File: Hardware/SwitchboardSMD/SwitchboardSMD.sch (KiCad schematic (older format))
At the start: 40 parts, among them J2 S88_In_Plug, J4 S88_Out_Plug, Q1 BC237, SW1 SW_Push, SW2 SW_Push, SW3 SW_Push, SW4 SW_Push, SW5 SW_Push, SW6 SW_Push, SW7 SW_Push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

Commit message: Fixed IC footprints
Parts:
- U1, U2, U3: footprint Package_SO:SOP-16_4.55x10.3mm_P1.27mm -> Package_SO:SOIC-16_3.9x9.9mm_P1.27mm
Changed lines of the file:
@@
 F 0 "U1" H 5100 2816 50  0000 C CNN
 F 1 "4044" H 5100 2725 50  0000 C CNN
-F 2 "Package_SO:SOP-16_4.55x10.3mm_P1.27mm" H 5100 2200 50  0001 C CNN
+F 2 "Package_SO:SOIC-16_3.9x9.9mm_P1.27mm" H 5100 2200 50  0001 C CNN
 F 3 "" H 5100 2200 50  0001 C CNN
 	1    5100 2200
@@
 F 0 "U3" H 7600 2756 50  0000 C CNN
 F 1 "4014" H 7600 2665 50  0000 C CNN
-F 2 "Package_SO:SOP-16_4.55x10.3mm_P1.27mm" H 7600 2200 50  0001 C CNN
+F 2 "Package_SO:SOIC-16_3.9x9.9mm_P1.27mm" H 7600 2200 50  0001 C CNN
 F 3 "" H 7600 2200 50  0001 C CNN
 	1    7600 2200
@@
 F 0 "U2" H 5100 4616 50  0000 C CNN
 F 1 "4044" H 5100 4525 50  0000 C CNN
-F 2 "Package_SO:SOP-16_4.55x10.3mm_P1.27mm" H 5100 4000 50  0001 C CNN
+F 2 "Package_SO:SOIC-16_3.9x9.9mm_P1.27mm" H 5100 4000 50  0001 C CNN
 F 3 "" H 5100 4000 50  0001 C CNN
 	1    5100 4000

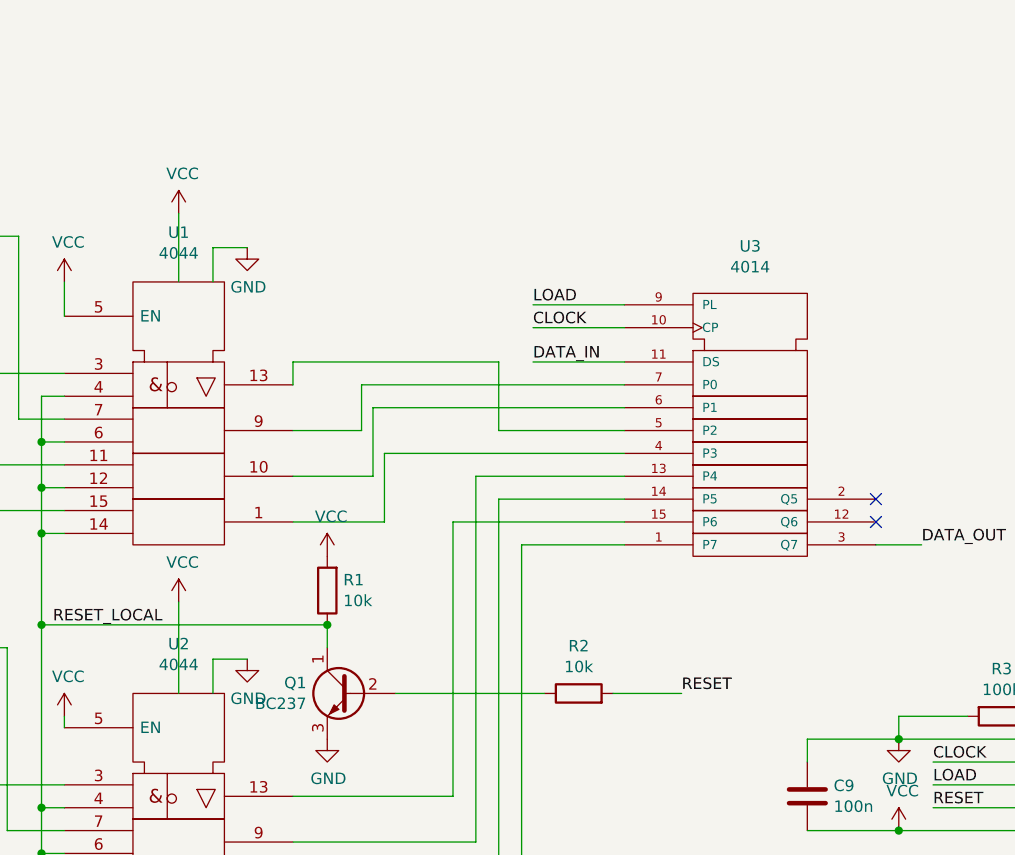
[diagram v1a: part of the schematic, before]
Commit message: Fixed inverted power connections for shift register
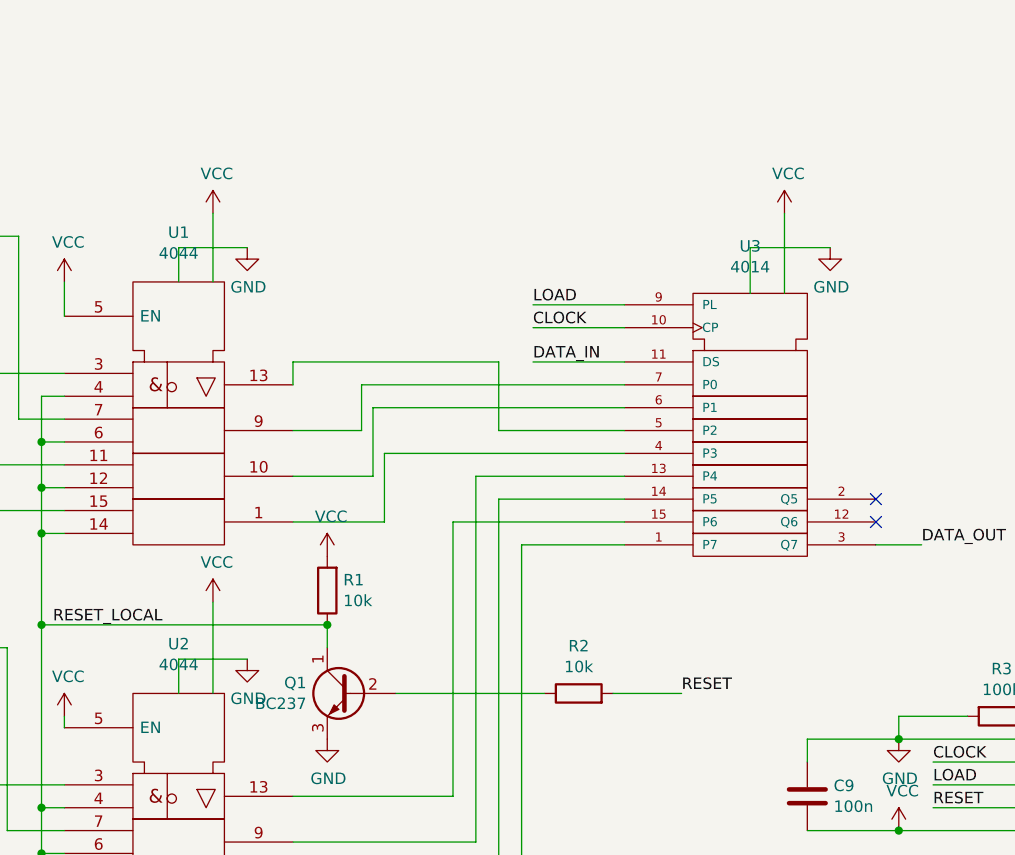
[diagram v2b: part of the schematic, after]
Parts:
- J2: footprint Connector_PinSocket_2.54mm:PinSocket_1x06_P2.54mm_Vertical -> Connector_PinSocket_2.00mm:PinSocket_1x06_P2.00mm_Horizontal
- J4: footprint Connector_PinHeader_2.54mm:PinHeader_1x06_P2.54mm_Vertical -> Connector_PinHeader_2.00mm:PinHeader_1x06_P2.00mm_Horizontal
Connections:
- wire segments 211 -> 214
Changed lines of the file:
@@
 F 0 "J2" H 10330 3892 50  0000 L CNN
 F 1 "S88_In_Plug" H 10330 3801 50  0000 L CNN
-F 2 "Connector_PinSocket_2.54mm:PinSocket_1x06_P2.54mm_Vertical" H 10250 3900 50  0001 C CNN
+F 2 "Connector_PinSocket_2.00mm:PinSocket_1x06_P2.00mm_Horizontal" H 10250 3900 50  0001 C CNN
 F 3 "~" H 10250 3900 50  0001 C CNN
 	1    10250 3900
@@
 F 0 "J4" H 10330 5292 50  0000 L CNN
 F 1 "S88_Out_Plug" H 10330 5201 50  0000 L CNN
-F 2 "Connector_PinHeader_2.54mm:PinHeader_1x06_P2.54mm_Vertical" H 10250 5300 50  0001 C CNN
+F 2 "Connector_PinHeader_2.00mm:PinHeader_1x06_P2.00mm_Horizontal" H 10250 5300 50  0001 C CNN
 F 3 "~" H 10250 5300 50  0001 C CNN
 	1    10250 5300
@@
 $EndComp
 Wire Wire Line
-	5250 3600 5250 3450
-Wire Wire Line
-	5250 3450 5400 3450
+	5250 3600 5250 3200
 $Comp
 L power:GND #PWR0102
@@
 	1    0    0    -1
 $EndComp
-Wire Wire Line
-	5250 1800 5250 1650
-Wire Wire Line
-	5250 1650 5400 1650
 $Comp
 L power:VCC #PWR0103
 U 1 1 5E592736
-P 5100 3200
-F 0 "#PWR0103" H 5100 3050 50  0001 C CNN
-F 1 "VCC" H 5117 3373 50  0000 C CNN
-F 2 "" H 5100 3200 50  0001 C CNN
-F 3 "" H 5100 3200 50  0001 C CNN
-	1    5100 3200
+P 5250 3200
+F 0 "#PWR0103" H 5250 3050 50  0001 C CNN
+F 1 "VCC" H 5267 3373 50  0000 C CNN
+F 2 "" H 5250 3200 50  0001 C CNN
+F 3 "" H 5250 3200 50  0001 C CNN
+	1    5250 3200
 	1    0    0    -1
 $EndComp
@@
 L power:VCC #PWR0104
 U 1 1 5E592A48
-P 5100 1500
-F 0 "#PWR0104" H 5100 1350 50  0001 C CNN
-F 1 "VCC" H 5117 1673 50  0000 C CNN
-F 2 "" H 5100 1500 50  0001 C CNN
-F 3 "" H 5100 1500 50  0001 C CNN
-	1    5100 1500
-	1    0    0    -1
-$EndComp
-Wire Wire Line
-	5100 1800 5100 1500
-Wire Wire Line
-	5100 3600 5100 3200
+P 5250 1500
+F 0 "#PWR0104" H 5250 1350 50  0001 C CNN
+F 1 "VCC" H 5267 1673 50  0000 C CNN
+F 2 "" H 5250 1500 50  0001 C CNN
+F 3 "" H 5250 1500 50  0001 C CNN
+	1    5250 1500
+	1    0    0    -1
+$EndComp
+Wire Wire Line
+	5100 3600 5100 3450
 $Comp
 L Device:R R5
@@
 Text Label 4550 3300 0    50   ~ 0
 RESET_LOCAL
+Wire Wire Line
+	5250 1800 5250 1500
+Wire Wire Line
+	5400 1650 5100 1650
+Wire Wire Line
+	5100 1650 5100 1800
+Wire Wire Line
+	5100 3450 5400 3450
+$Comp
+L power:VCC #PWR0105
+U 1 1 5EF73F90
+P 7750 1500
+F 0 "#PWR0105" H 7750 1350 50  0001 C CNN
+F 1 "VCC" H 7767 1673 50  0000 C CNN
+F 2 "" H 7750 1500 50  0001 C CNN
+F 3 "" H 7750 1500 50  0001 C CNN
+	1    7750 1500
+	1    0    0    -1
+$EndComp
+$Comp
+L power:GND #PWR0106
+U 1 1 5EF74698
+P 7950 1650
+F 0 "#PWR0106" H 7950 1400 50  0001 C CNN
+F 1 "GND" H 7955 1477 50  0000 C CNN
+F 2 "" H 7950 1650 50  0001 C CNN
+F 3 "" H 7950 1650 50  0001 C CNN
+	1    7950 1650
+	1    0    0    -1
+$EndComp
+Wire Wire Line
+	7600 1850 7600 1650
+Wire Wire Line
+	7600 1650 7950 1650
+Wire Wire Line
+	7750 1850 7750 1500
 $EndSCHEMATC
